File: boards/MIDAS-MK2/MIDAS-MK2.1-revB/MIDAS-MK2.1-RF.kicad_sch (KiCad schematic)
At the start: 13 parts, among them J401 SMA, J402 SMA, Q401 Si1016X, U401 RFM96W-433S2, U402 NC7WZ07, U403 MAX-M10S

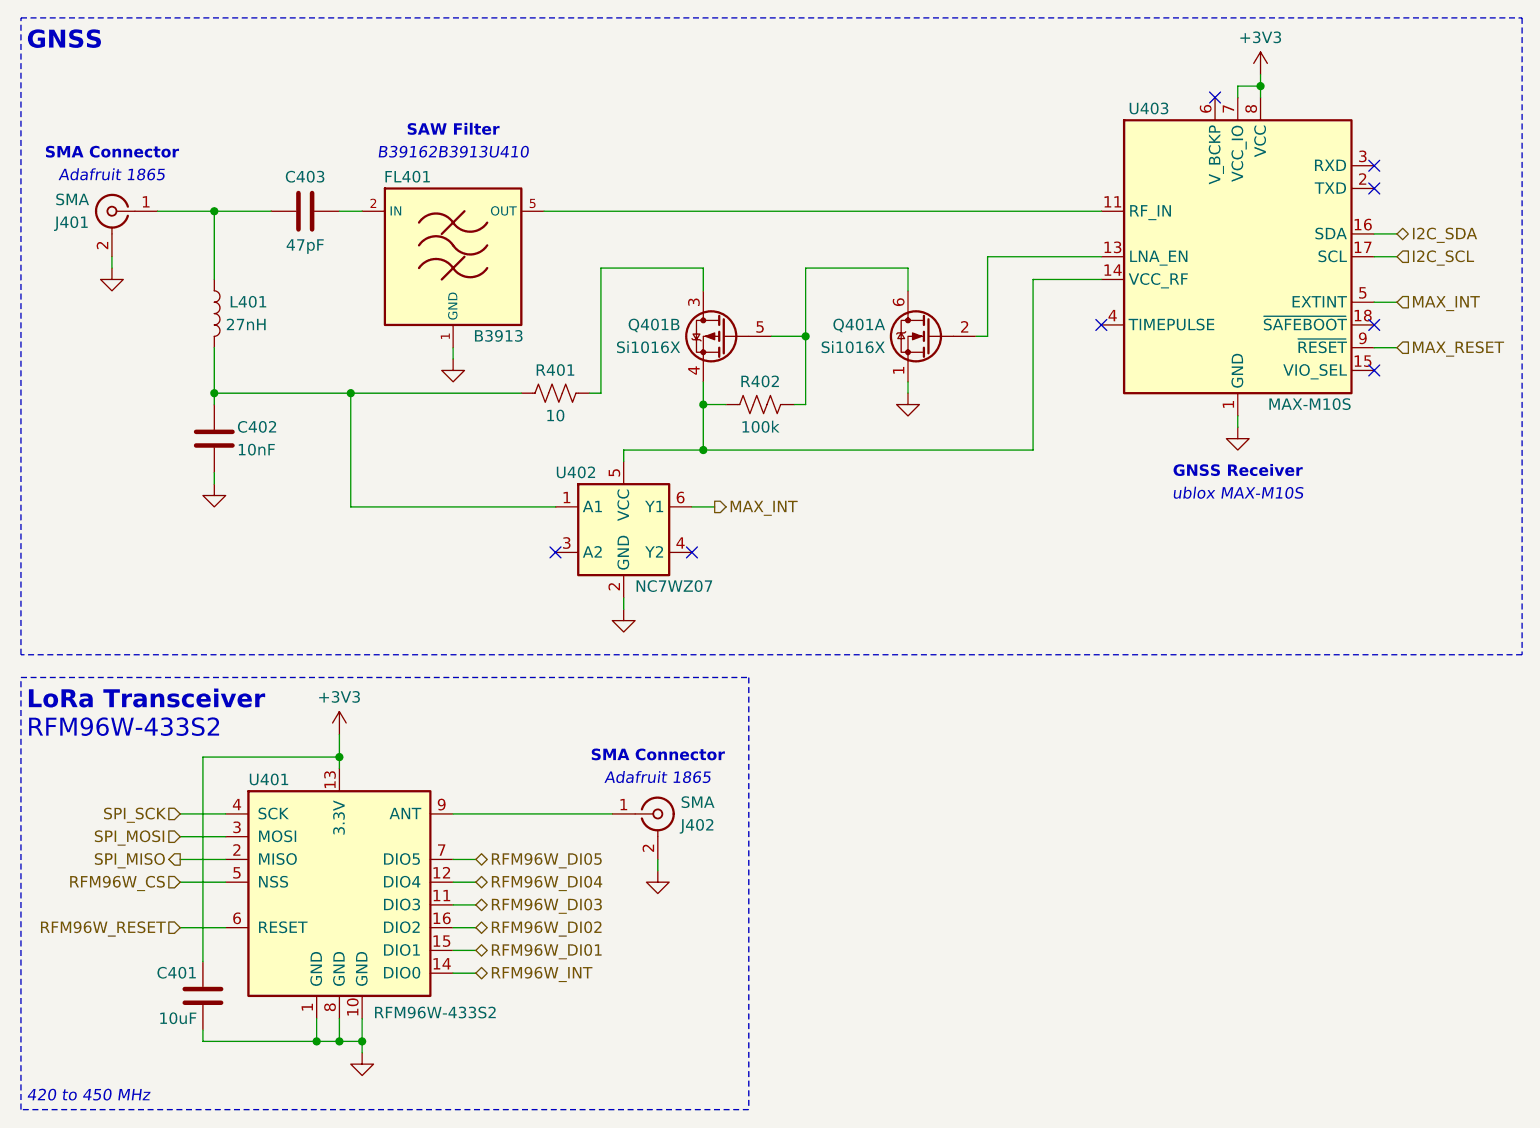
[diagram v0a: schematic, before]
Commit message: reverting stuff out of branches scope & deleting outdated images
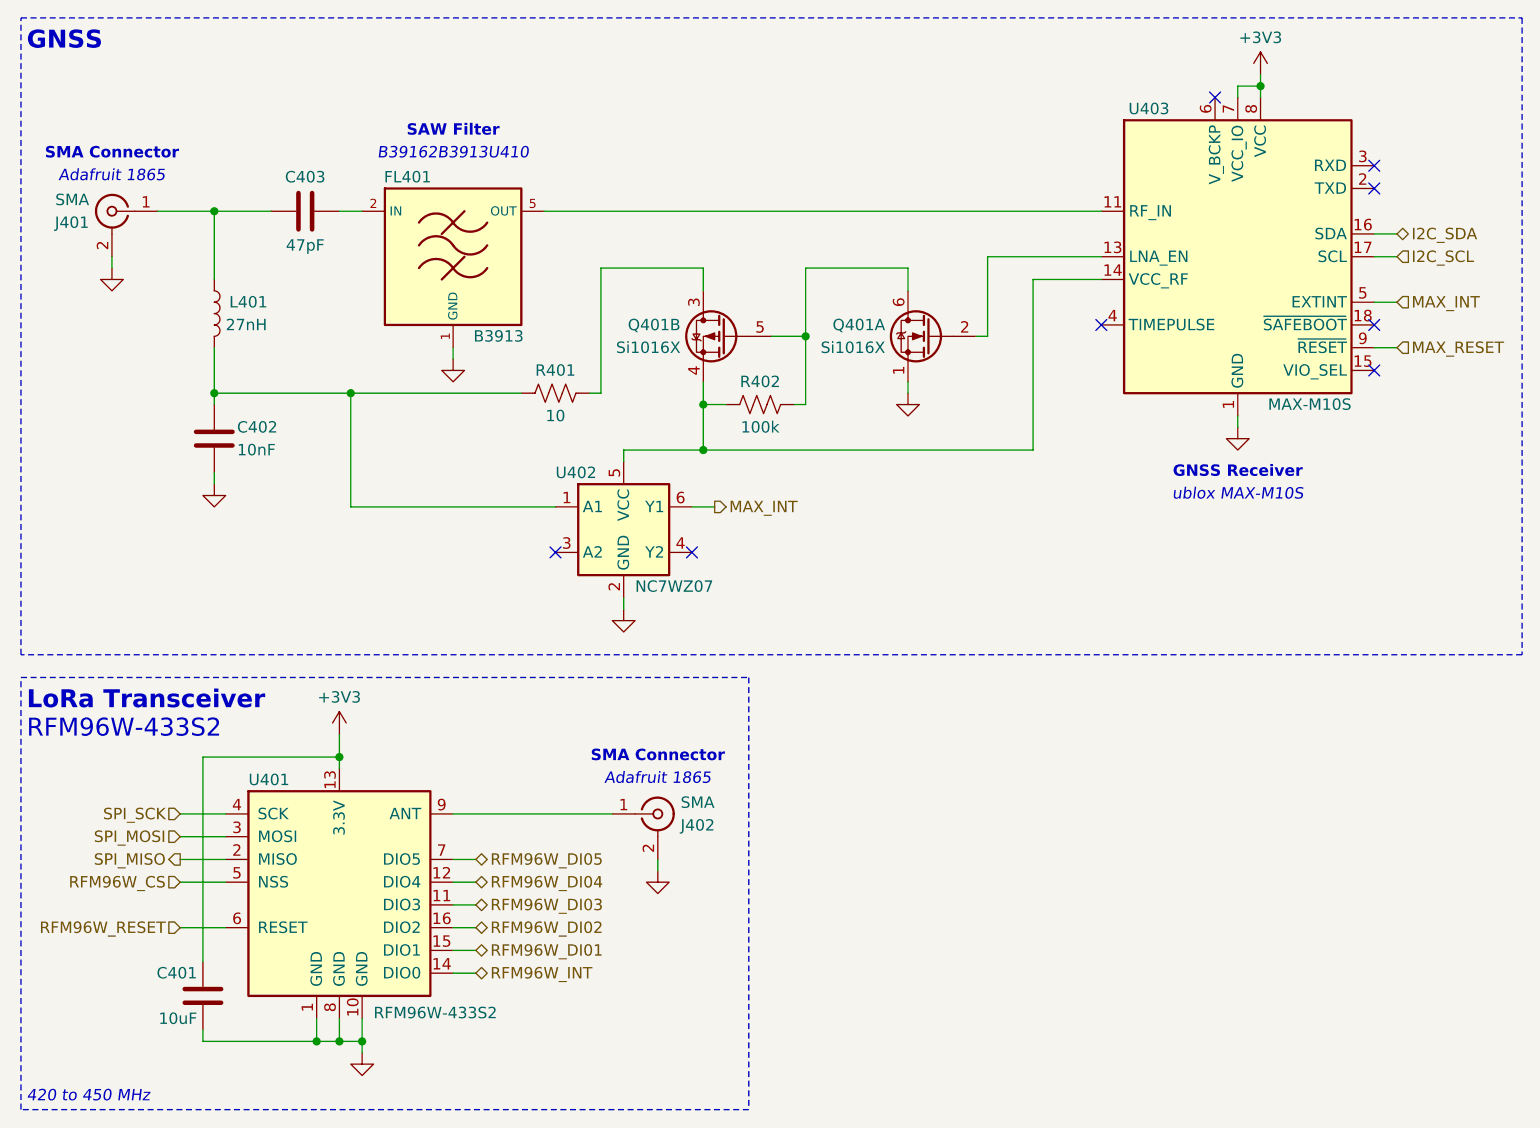
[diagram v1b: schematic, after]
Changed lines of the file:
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@@
 (kicad_sch
-	(version 20250114)
+	(version 20231120)
 	(generator "eeschema")
-	(generator_version "9.0")
+	(generator_version "8.0")
 	(paper "A3")
 	(title_block
@@
 		(comment 4 "Contributors: Thomas McManamen")
 	)
-	(rectangle
-		(start 15.24 15.24)
-		(end 182.88 86.36)
-		(stroke
-			(width 0)
-			(type dash)
-		)
-		(fill
-			(type none)
-		)
-	)
-	(rectangle
-		(start 15.24 88.9)
-		(end 96.52 137.16)
-		(stroke
-			(width 0)
-			(type dash)
-		)
-		(fill
-			(type none)
-		)
-	)
-	(text "B39162B3913U410"
-		(exclude_from_sim no)
-		(at 63.5 30.48 0)
-		(effects
-			(font
-				(size 1.27 1.27)
-				(italic yes)
-			)
-		)
-	)
-	(text "Adafruit 1865"
-		(exclude_from_sim no)
-		(at 86.36 100.33 0)
-		(effects
-			(font
-				(size 1.27 1.27)
-				(italic yes)
-			)
-		)
-	)
-	(text "Adafruit 1865"
-		(exclude_from_sim no)
-		(at 25.4 33.02 0)
-		(effects
-			(font
-				(size 1.27 1.27)
-				(italic yes)
-			)
-		)
-	)
-	(text "420 to 450 MHz"
-		(exclude_from_sim no)
-		(at 15.875 136.525 0)
-		(effects
-			(font
-				(size 1.27 1.27)
-				(italic yes)
-			)
-			(justify left bottom)
-		)
-	)
-	(text "GNSS Receiver"
-		(exclude_from_sim no)
-		(at 151.13 66.04 0)
-		(effects
-			(font
-				(size 1.27 1.27)
-				(thickness 0.254)
-				(bold yes)
-			)
-		)
-	)
-	(text "SMA Connector"
-		(exclude_from_sim no)
-		(at 25.4 30.48 0)
-		(effects
-			(font
-				(size 1.27 1.27)
-				(thickness 0.254)
-				(bold yes)
-			)
-		)
-	)
-	(text "RFM96W-433S2"
-		(exclude_from_sim no)
-		(at 15.875 95.885 0)
-		(effects
-			(font
-				(size 2 2)
-			)
-			(justify left bottom)
-		)
-	)
-	(text "SAW Filter"
-		(exclude_from_sim no)
-		(at 63.5 27.94 0)
-		(effects
-			(font
-				(size 1.27 1.27)
-				(thickness 0.254)
-				(bold yes)
-			)
-		)
-	)
-	(text "SMA Connector"
-		(exclude_from_sim no)
-		(at 86.36 97.79 0)
-		(effects
-			(font
-				(size 1.27 1.27)
-				(thickness 0.254)
-				(bold yes)
-			)
-		)
-	)
-	(text "GNSS"
-		(exclude_from_sim no)
-		(at 15.875 19.05 0)
-		(effects
-			(font
-				(size 2 2)
-				(thickness 0.4)
-				(bold yes)
-			)
-			(justify left bottom)
-		)
-	)
-	(text "ublox MAX-M10S"
-		(exclude_from_sim no)
-		(at 151.13 68.58 0)
-		(effects
-			(font
-				(size 1.27 1.27)
-				(italic yes)
-			)
-		)
-	)
-	(text "LoRa Transceiver"
-		(exclude_from_sim no)
-		(at 15.875 92.71 0)
-		(effects
-			(font
-				(size 2 2)
-				(bold yes)
-			)
-			(justify left bottom)
-		)
-	)
 	(junction
 		(at 91.44 58.42)
@@
 		)
 	)
+	(rectangle
+		(start 15.24 15.24)
+		(end 182.88 86.36)
+		(stroke
+			(width 0)
+			(type dash)
+		)
+		(fill
+			(type none)
+		)
+	)
+	(rectangle
+		(start 15.24 88.9)
+		(end 96.52 137.16)
+		(stroke
+			(width 0)
+			(type dash)
+		)
+		(fill
+			(type none)
+		)
+	)
+	(text "B39162B3913U410"
+		(exclude_from_sim no)
+		(at 63.5 30.48 0)
+		(effects
+			(font
+				(size 1.27 1.27)
+				(italic yes)
+			)
+		)
+	)
+	(text "Adafruit 1865"
+		(exclude_from_sim no)
+		(at 86.36 100.33 0)
+		(effects
+			(font
+				(size 1.27 1.27)
+				(italic yes)
+			)
+		)
+	)
+	(text "Adafruit 1865"
+		(exclude_from_sim no)
+		(at 25.4 33.02 0)
+		(effects
+			(font
+				(size 1.27 1.27)
+				(italic yes)
+			)
+		)
+	)
+	(text "420 to 450 MHz"
+		(exclude_from_sim no)
+		(at 15.875 136.525 0)
+		(effects
+			(font
+				(size 1.27 1.27)
+				(italic yes)
+			)
+			(justify left bottom)
+		)
+	)
+	(text "GNSS Receiver"
+		(exclude_from_sim no)
+		(at 151.13 66.04 0)
+		(effects
+			(font
+				(size 1.27 1.27)
+				(thickness 0.254)
+				(bold yes)
+			)
+		)
+	)
+	(text "SMA Connector"
+		(exclude_from_sim no)
+		(at 25.4 30.48 0)
+		(effects
+			(font
+				(size 1.27 1.27)
+				(thickness 0.254)
+				(bold yes)
+			)
+		)
+	)
+	(text "RFM96W-433S2"
+		(exclude_from_sim no)
+		(at 15.875 95.885 0)
+		(effects
+			(font
+				(size 2 2)
+			)
+			(justify left bottom)
+		)
+	)
+	(text "SAW Filter"
+		(exclude_from_sim no)
+		(at 63.5 27.94 0)
+		(effects
+			(font
+				(size 1.27 1.27)
+				(thickness 0.254)
+				(bold yes)
+			)
+		)
+	)
+	(text "SMA Connector"
+		(exclude_from_sim no)
+		(at 86.36 97.79 0)
+		(effects
+			(font
+				(size 1.27 1.27)
+				(thickness 0.254)
+				(bold yes)
+			)
+		)
+	)
+	(text "GNSS"
+		(exclude_from_sim no)
+		(at 15.875 19.05 0)
+		(effects
+			(font
+				(size 2 2)
+				(thickness 0.4)
+				(bold yes)
+			)
+			(justify left bottom)
+		)
+	)
+	(text "ublox MAX-M10S"
+		(exclude_from_sim no)
+		(at 151.13 68.58 0)
+		(effects
+			(font
+				(size 1.27 1.27)
+				(italic yes)
+			)
+		)
+	)
+	(text "LoRa Transceiver"
+		(exclude_from_sim no)
+		(at 15.875 92.71 0)
+		(effects
+			(font
+				(size 2 2)
+				(bold yes)
+			)
+			(justify left bottom)
+		)
+	)
 	(hierarchical_label "SPI_SCK"
 		(shape input)
 		(at 33.02 104.14 180)
+		(fields_autoplaced yes)
 		(effects
 			(font
@@
 		(shape output)
 		(at 33.02 109.22 180)
+		(fields_autoplaced yes)
 		(effects
 			(font
@@
 		(shape input)
 		(at 168.91 52.07 0)
+		(fields_autoplaced yes)
 		(effects
 			(font
@@
 		(shape input)
 		(at 168.91 46.99 0)
+		(fields_autoplaced yes)
 		(effects
 			(font
@@
 		(shape bidirectional)
 		(at 66.04 109.22 0)
+		(fields_autoplaced yes)
 		(effects
 			(font
@@
 		(shape input)
 		(at 33.02 116.84 180)
+		(fields_autoplaced yes)
 		(effects
 			(font
@@
 		(shape input)
 		(at 33.02 111.76 180)
+		(fields_autoplaced yes)
 		(effects
 			(font
@@
 		(shape output)
 		(at 92.71 69.85 0)
+		(fields_autoplaced yes)
 		(effects
 			(font
@@
 		(shape bidirectional)
 		(at 66.04 121.92 0)
+		(fields_autoplaced yes)
 		(effects
 			(font
@@
 		(shape bidirectional)
 		(at 168.91 39.37 0)
+		(fields_autoplaced yes)
 		(effects
 			(font
@@
 		(shape bidirectional)
 		(at 66.04 111.76 0)
+		(fields_autoplaced yes)
 		(effects
 			(font
@@
 		(shape input)
 		(at 33.02 106.68 180)
+		(fields_autoplaced yes)
 		(effects
 			(font
@@
 		(shape bidirectional)
 		(at 66.04 119.38 0)
+		(fields_autoplaced yes)
 		(effects
 			(font
@@
 		(shape bidirectional)
 		(at 66.04 114.3 0)
+		(fields_autoplaced yes)
 		(effects
 			(font
@@
 		(shape bidirectional)
 		(at 66.04 116.84 0)
+		(fields_autoplaced yes)
 		(effects
 			(font
@@
 		(shape input)
 		(at 168.91 41.91 0)
-		(effects
-			(font
+		(fields_autoplaced yes)
+		(effects
+			(font
